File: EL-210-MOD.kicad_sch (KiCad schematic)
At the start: 29 parts, among them J1 Conn_01x05, J2 Conn_01x02, P1 EL-210-KEY, U1 9-ST-20, U2 STM32G0B1KET6, U3 MAX6934AQH+D, U4 TPS613221ADBV, U5 MAX4719EUB+, U6 TLV61046ADB

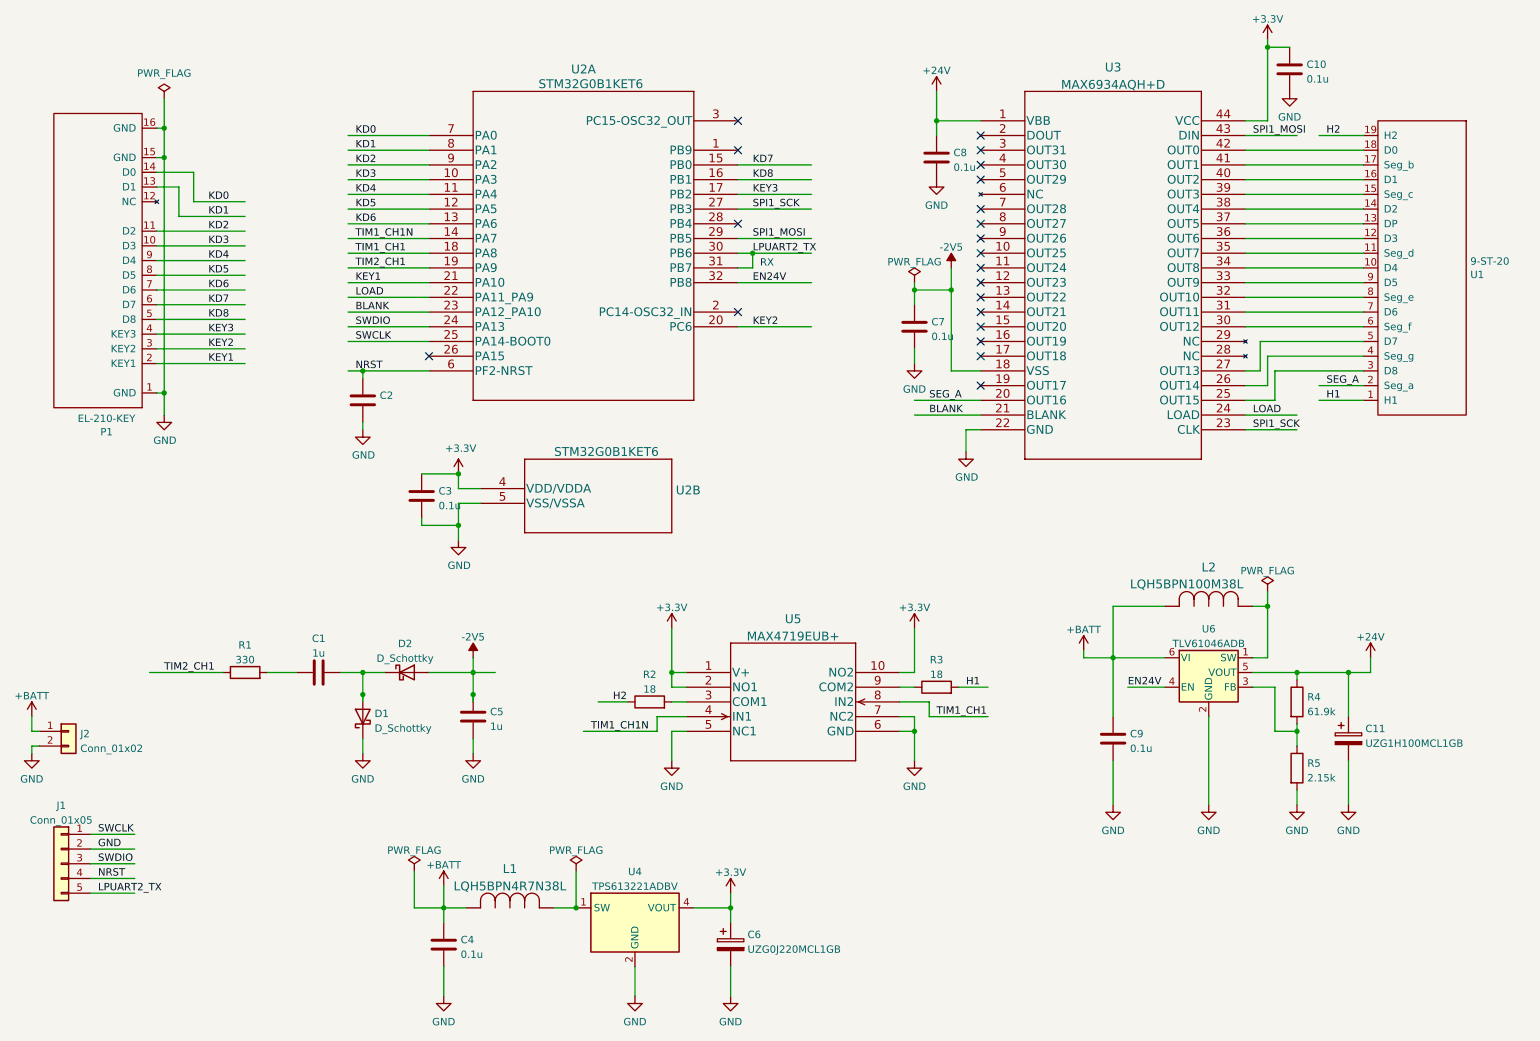
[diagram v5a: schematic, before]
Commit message: Schematics layout refined.
Added note on the Tc and R4/R5 expression.
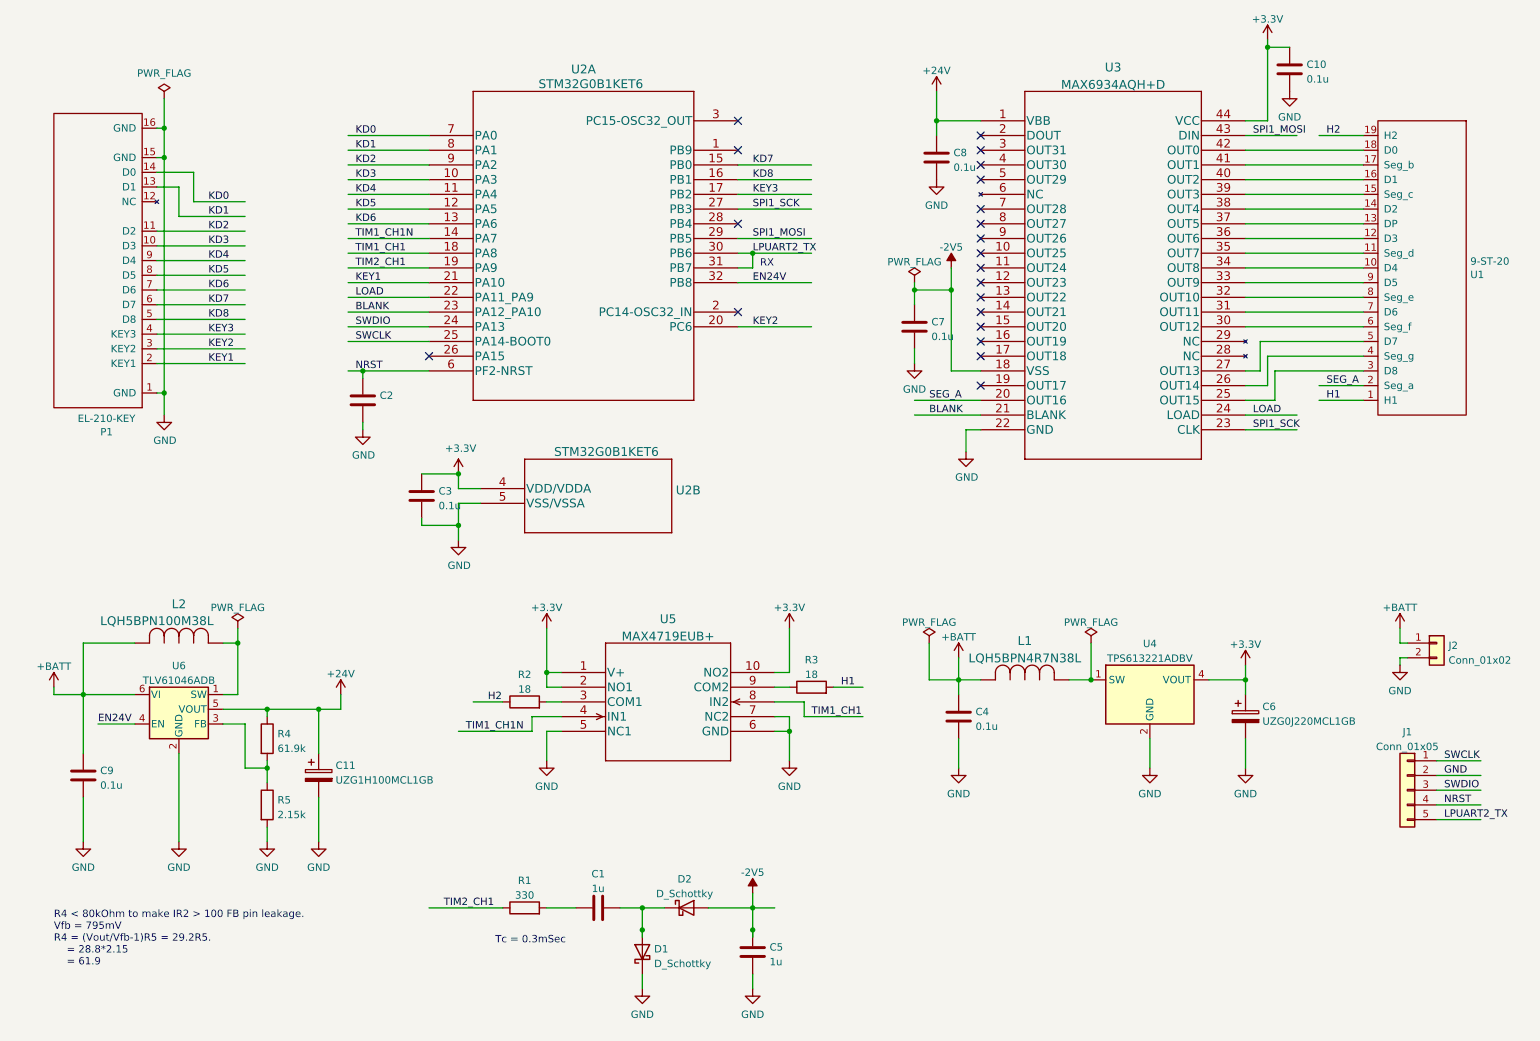
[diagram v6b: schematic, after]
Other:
- note added: "R4 < 80kOhm to make IR2 > 100 FB pin leakage. Vfb = 795mV R4 = (Vout/Vfb-1)R5 = 29.2R5. = 28.8*2.15 = 61.9"
- note added: "Tc = 0.3mSec"
- moved on the sheet: C1, C11, C4, C5, C6, C9, D1, D2, J1, J2, L1, L2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

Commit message: Layout refined.
Higher parts are moved to the front side to avoid the
touch with the back cabinet.
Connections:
- net KD0: now also U2.21 (PA10); no longer U2.7 (PA0)
- net KD1: now also U2.20 (PC6); no longer U2.8 (PA1)
- net KD2: now also U2.17 (PB2); no longer U2.9 (PA2)
- net KD3: now also U2.16 (PB1); no longer U2.10 (PA3)
- net KD4: now also U2.15 (PB0); no longer U2.11 (PA4)
- net KD5: now also U2.13 (PA6); no longer U2.12 (PA5)
- net KD6: now also U2.12 (PA5); no longer U2.13 (PA6)
- net KD7: now also U2.11 (PA4); no longer U2.15 (PB0)
- net KD8: now also U2.10 (PA3); no longer U2.16 (PB1)
- net KEY1: now also U2.7 (PA0); no longer U2.21 (PA10)
- net KEY2: now also U2.8 (PA1); no longer U2.20 (PC6)
- net KEY3: now also U2.9 (PA2); no longer U2.17 (PB2)
- net at U1.10 (D4): now also U3.35 (OUT7); no longer U3.34 (OUT8)
- net at U1.11 (Seg_d): now also U3.34 (OUT8); no longer U3.35 (OUT7)
- net at U1.12 (D3): now also U3.33 (OUT9); no longer U3.36 (OUT6)
- net at U1.13 (DP): now also U3.32 (OUT10); no longer U3.37 (OUT5)
- net at U1.14 (D2): now also U3.31 (OUT11); no longer U3.38 (OUT4)
- net at U1.15 (Seg_c): now also U3.30 (OUT12); no longer U3.39 (OUT3)
- net at U1.16 (D1): now also U3.27 (OUT13); no longer U3.40 (OUT2)
- net at U1.17 (Seg_b): now also U3.26 (OUT14); no longer U3.41 (OUT1)
- net at U1.18 (D0): now also U3.25 (OUT15); no longer U3.42 (OUT0)
- net at U1.3 (D8): now also U3.42 (OUT0); no longer U3.25 (OUT15)
- net at U1.4 (Seg_g): now also U3.41 (OUT1); no longer U3.26 (OUT14)
- net at U1.5 (D7): now also U3.40 (OUT2); no longer U3.27 (OUT13)
- net at U1.6 (Seg_f): now also U3.39 (OUT3); no longer U3.30 (OUT12)
- net at U1.7 (D6): now also U3.38 (OUT4); no longer U3.31 (OUT11)
- net at U1.8 (Seg_e): now also U3.37 (OUT5); no longer U3.32 (OUT10)
- net at U1.9 (D5): now also U3.36 (OUT6); no longer U3.33 (OUT9)
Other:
- moved on the sheet: U1
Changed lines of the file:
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@@
     (stroke (width 0) (type default) (color 0 0 0 0))
   )
-  (wire (pts (xy 254 81.28) (xy 246.38 81.28))
+  (wire (pts (xy 254 38.1) (xy 246.38 38.1))
     (stroke (width 0) (type default) (color 0 0 0 0))
   )
@@
     (stroke (width 0) (type default) (color 0 0 0 0))
   )
-  (wire (pts (xy 246.38 83.82) (xy 254 83.82))
+  (wire (pts (xy 246.38 35.56) (xy 254 35.56))
     (stroke (width 0) (type default) (color 0 0 0 0))
   )
@@
     (stroke (width 0) (type default) (color 0 0 0 0))
   )
-  (wire (pts (xy 246.38 38.1) (xy 254 38.1))
+  (wire (pts (xy 246.38 81.28) (xy 254 81.28))
     (stroke (width 0) (type default) (color 0 0 0 0))
   )
@@
     (effects (font (size 1.27 1.27)) (justify left bottom))
   )
-  (label "KEY2" (at 148.59 71.12 0)
+  (label "KEY2" (at 80.01 40.64 0)
     (effects (font (size 1.27 1.27)) (justify left bottom))
   )
@@
     (effects (font (size 1.27 1.27)) (justify left bottom))
   )
-  (label "KD7" (at 148.59 43.18 0)
+  (label "KD7" (at 80.01 48.26 0)
     (effects (font (size 1.27 1.27)) (justify left bottom))
   )
@@
     (effects (font (size 1.27 1.27)) (justify left bottom))
   )
-  (label "KD0" (at 80.01 38.1 0)
-    (effects (font (size 1.27 1.27)) (justify left bottom))
-  )
-  (label "KD8" (at 148.59 45.72 0)
+  (label "KD0" (at 80.01 63.5 0)
+    (effects (font (size 1.27 1.27)) (justify left bottom))
+  )
+  (label "KD8" (at 80.01 45.72 0)
     (effects (font (size 1.27 1.27)) (justify left bottom))
   )
@@
     (effects (font (size 1.27 1.27)) (justify left bottom))
   )
-  (label "KD5" (at 80.01 50.8 0)
+  (label "KD5" (at 80.01 53.34 0)
     (effects (font (size 1.27 1.27)) (justify left bottom))
   )
@@
     (effects (font (size 1.27 1.27)) (justify left bottom))
   )
-  (label "KD4" (at 80.01 48.26 0)
+  (label "KD4" (at 148.59 43.18 0)
     (effects (font (size 1.27 1.27)) (justify left bottom))
   )
@@
     (effects (font (size 1.27 1.27)) (justify left bottom))
   )
-  (label "H1" (at 247.65 83.82 0)
+  (label "H1" (at 247.65 35.56 0)
     (effects (font (size 1.27 1.27)) (justify left bottom))
   )
@@
     (effects (font (size 1.27 1.27)) (justify left bottom))
   )
-  (label "KEY3" (at 148.59 48.26 0)
+  (label "KEY3" (at 80.01 43.18 0)
     (effects (font (size 1.27 1.27)) (justify left bottom))
   )
@@
     (effects (font (size 1.27 1.27)) (justify left bottom))
   )
-  (label "KEY1" (at 80.01 63.5 0)
-    (effects (font (size 1.27 1.27)) (justify left bottom))
-  )
-  (label "KD6" (at 80.01 53.34 0)
+  (label "KEY1" (at 80.01 38.1 0)
+    (effects (font (size 1.27 1.27)) (justify left bottom))
+  )
+  (label "KD6" (at 80.01 50.8 0)
     (effects (font (size 1.27 1.27)) (justify left bottom))
   )
@@
     (effects (font (size 1.27 1.27)) (justify left bottom))
   )
-  (label "KD3" (at 80.01 45.72 0)
-    (effects (font (size 1.27 1.27)) (justify left bottom))
-  )
-  (label "SEG_A" (at 247.65 81.28 0)
+  (label "KD3" (at 148.59 45.72 0)
+    (effects (font (size 1.27 1.27)) (justify left bottom))
+  )
+  (label "SEG_A" (at 247.65 38.1 0)
     (effects (font (size 1.27 1.27)) (justify left bottom))
   )
@@
     (effects (font (size 1.27 1.27)) (justify left bottom))
   )
-  (label "KD2" (at 80.01 43.18 0)
+  (label "KD2" (at 148.59 48.26 0)
     (effects (font (size 1.27 1.27)) (justify left bottom))
   )
@@
     (effects (font (size 1.27 1.27)) (justify left bottom))
   )
-  (label "KD1" (at 80.01 40.64 0)
+  (label "KD1" (at 148.59 71.12 0)
     (effects (font (size 1.27 1.27)) (justify left bottom))
   )
@@
     (effects (font (size 1.27 1.27)) (justify left bottom))
   )
-  (label "H2" (at 247.65 38.1 0)
+  (label "H2" (at 248.92 81.28 0)
     (effects (font (size 1.27 1.27)) (justify left bottom))
   )
@@
     (pin "9")
   )
-  (symbol (lib_id "9-ST-20:9-ST-20") (at 256.54 83.82 0) (mirror x) (unit 1)
+  (symbol (lib_id "9-ST-20:9-ST-20") (at 256.54 35.56 0) (unit 1)
     (in_bom yes) (on_board yes)
-    (property "Reference" "U1" (id 0) (at 272.4912 62.1284 0)
+    (property "Reference" "U1" (id 0) (at 272.4912 57.2516 0)
       (effects (font (size 1.27 1.27)) (justify left))
     )
-    (property "Value" "9-ST-20" (id 1) (at 272.4912 59.817 0)
+    (property "Value" "9-ST-20" (id 1) (at 272.4912 59.563 0)
       (effects (font (size 1.27 1.27)) (justify left))
     )
-    (property "Footprint" "9-ST-20:9-ST-20" (id 2) (at 256.54 83.82 0)
+    (property "Footprint" "9-ST-20:9-ST-20" (id 2) (at 256.54 35.56 0)
       (effects (font (size 1.27 1.27)) hide)
     )
-    (property "Datasheet" "" (id 3) (at 256.54 83.82 0)
+    (property "Datasheet" "" (id 3) (at 256.54 35.56 0)
       (effects (font (size 1.27 1.27)) hide)
     )
